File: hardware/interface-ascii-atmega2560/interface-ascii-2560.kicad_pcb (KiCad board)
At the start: 2 copper layers, 88.9 x 132.1 mm, 46 parts, among them J1 Apple 2, J2 Apple 1, J3 UART, J4 Conn_01x05, J5 SOL-20, J6 ISP header, J7 Keyboard, SW1 Options, U1 ATmega2560-16AU, Y1 16.000 MHz

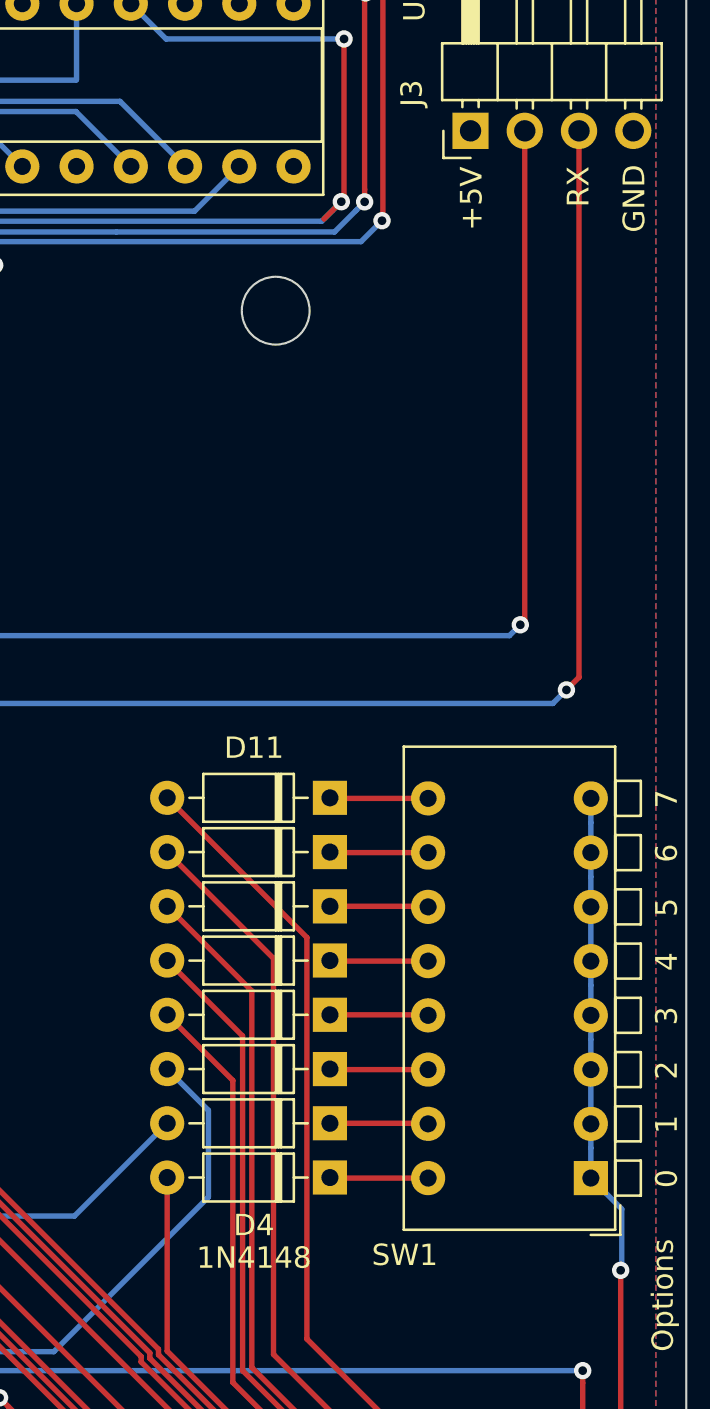
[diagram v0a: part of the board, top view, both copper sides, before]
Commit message: Silk screen cleanups
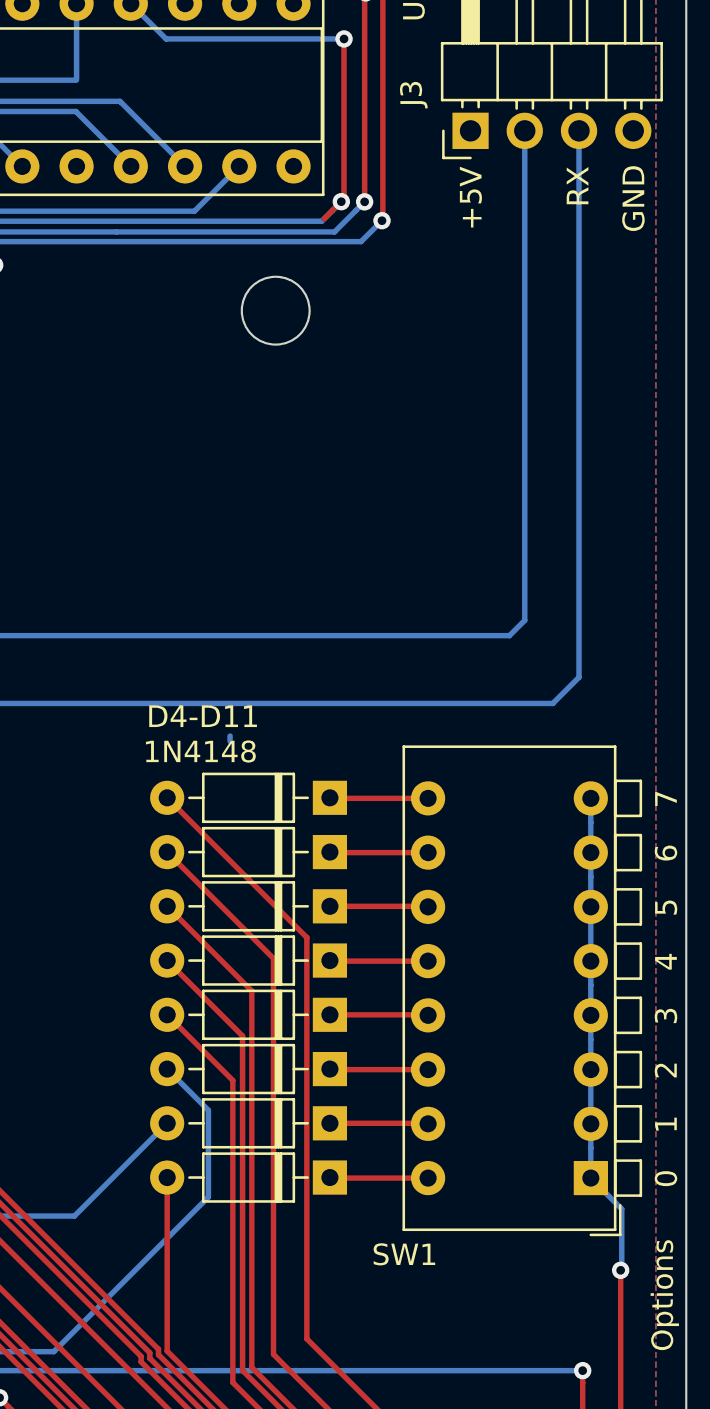
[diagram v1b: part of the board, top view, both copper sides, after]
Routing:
- net /Tx: vias 2 -> 1
- net /Rx: vias 2 -> 1
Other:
- board text added: "D4-D11"

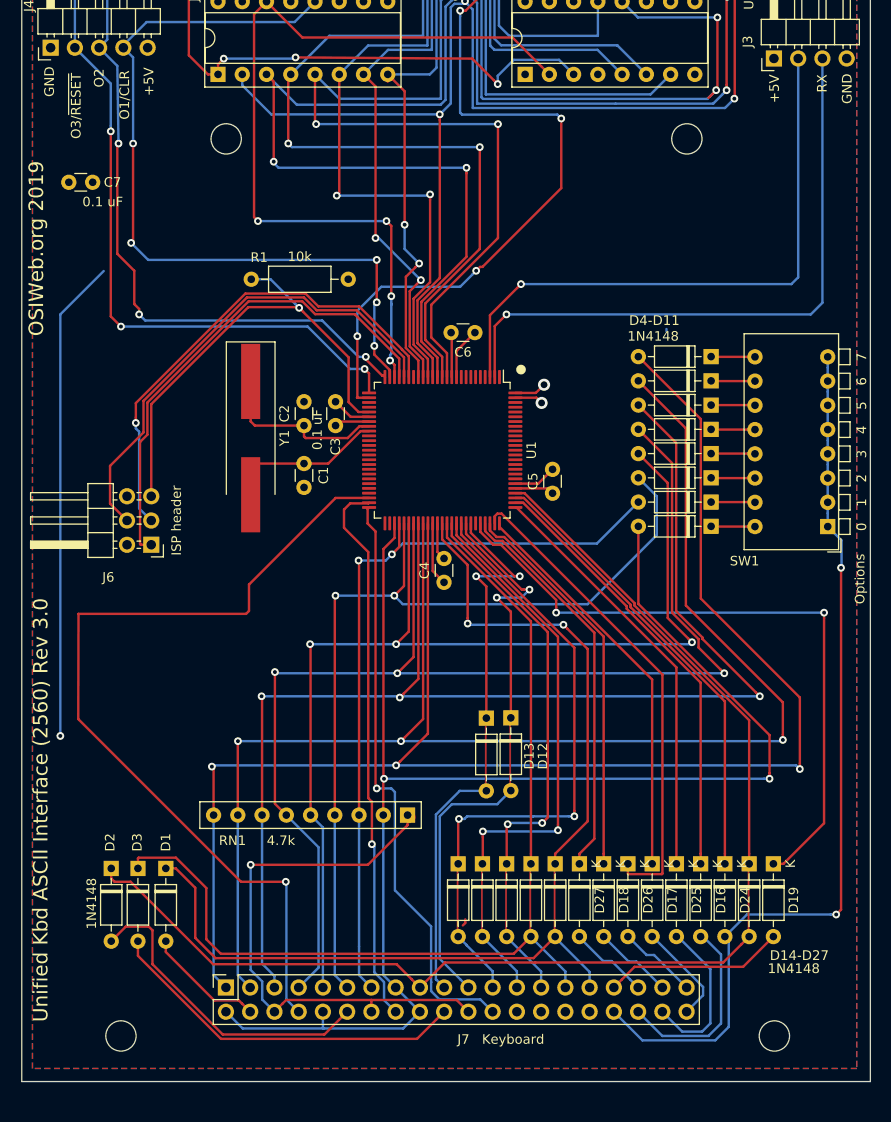
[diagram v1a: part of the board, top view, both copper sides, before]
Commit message: Add 16-pin socket for custom interface/prototyping
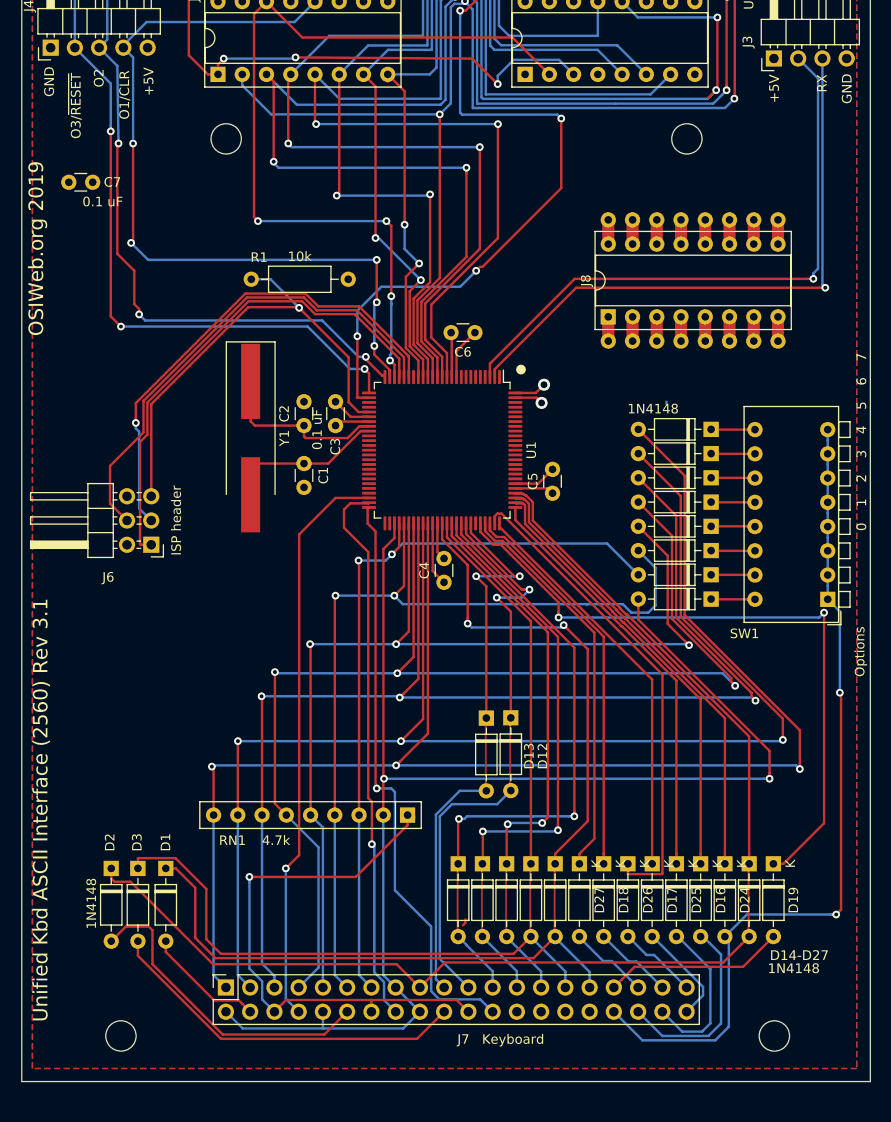
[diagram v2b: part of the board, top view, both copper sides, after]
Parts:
- added J8: Custom Connector / Proto, unikbd:DIP-16_W7.62mm_Proto, F.Cu at (225.3, 102.8)
- moved D10 7.62 mm to (236.0, 117.1)
- moved D11 7.62 mm to (236.0, 114.6)
- moved D4 7.62 mm to (236.0, 132.3)
- moved D5 7.62 mm to (236.0, 129.8)
- moved D6 7.62 mm to (236.0, 127.3)
- moved D8 7.62 mm to (236.0, 122.2)
- moved D7 7.62 mm to (236.0, 124.7)
- moved D9 7.62 mm to (236.0, 119.6)
- moved SW1 7.62 mm to (248.3, 132.4)
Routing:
- net Net-(R2-Pad1): track 50.6 -> 0.00 mm, vias 1 -> 0
- net /LED1: track 91.0 -> 60.0 mm
- net /Col0: track 149.5 -> 141.4 mm
- net /Col3: track 111.9 -> 104.1 mm
- net /Col5: track 138.3 -> 130.5 mm
- net /Col7: track 162.5 -> 154.9 mm
- net /Col6: track 151.2 -> 143.5 mm
- net /Row8: track 95.2 -> 87.6 mm
- net /Col4: track 128.7 -> 124.5 mm
- net /Rx: track 66.3 -> 63.1 mm
- net /Col2: track 93.5 -> 90.9 mm
- net Net-(D19-Pad1): track 70.3 -> 70.9 mm
- net VCC: track 82.3 -> 81.7 mm
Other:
- board text added: "Unified Kbd ASCII Interface (2560) Rev 3.1"
- board text removed: "D4-D11"
- board text removed: "Unified Kbd ASCII Interface (2560) Rev 3.0"

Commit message: Clean up connector labels on ATmel-2560 ASCII interface PCB
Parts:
- added ?: , , F.Cu at (230.4, 88.2)
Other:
- board text added: "Custom Connector"
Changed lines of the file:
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@@
   (general
     (thickness 1.6)
-    (drawings 33)
+    (drawings 34)
     (tracks 1003)
     (zones 0)
-    (modules 47)
+    (modules 48)
     (nets 148)
   )
@@
     (add_net /Col0)
   )
+  (module "" (layer F.Cu)
+    (at 230.355 88.165)
+    (fp_text reference "" (at 225.275 102.77) (layer F.SilkS)
+      (effects (font (size 1.27 1.27) (thickness 0.15)))
+    )
+    (fp_text value "" (at 225.275 102.77) (layer F.SilkS)
+      (effects (font (size 1.27 1.27) (thickness 0.15)))
+    )
+    (fp_text user "Apple 1" (at 228.323 102.77 90) (layer F.SilkS)
+      (effects (font (size 1.27 1.27) (thickness 0.15)))
+    )
+  )
   (module unikbd:DIP-16_W7.62mm_Proto (layer F.Cu)
     (at 225.275 102.77 90)
     (descr "16-lead though-hole mounted DIP package, row spacing 7.62 mm (300 mils), Socket")
     (tags "THT DIP DIL PDIP 2.54mm 7.62mm 300mil Socket")
-    (fp_text reference J8 (at 3.81 -2.33 90) (layer F.SilkS)
+    (fp_text reference J8 (at 8.255 -3.175 180) (layer F.SilkS)
       (effects (font (size 1 1) (thickness 0.15)))
     )
@@
     )
     (fp_text value SOL-20 (at 5.1308 17.5514 180) (layer F.SilkS)
-      (effects (font (size 1 1) (thickness 0.15)))
+      (effects (font (size 1.27 1.27) (thickness 0.1524)))
     )
     (fp_text user %R (at 1.27 11.43) (layer F.Fab)
@@
       (effects (font (size 1 1) (thickness 0.15)))
     )
-    (fp_text value "Apple 2" (at 10.795 9.856168) (layer F.SilkS)
+    (fp_text value "Apple 2" (at 10.16 18.238168) (layer F.SilkS)
       (effects (font (size 1.27 1.27) (thickness 0.15)))
     )
@@
     )
     (fp_text value "Apple 1" (at 10.795 8.372834 180) (layer F.SilkS)
-      (effects (font (size 1.27 1.27) (thickness 0.15)))
+      (effects (font (size 1.27 1.27) (thickness 0.1524)))
     )
     (fp_text user %R (at 9.50214 -0.78486 180) (layer F.SilkS) hide
@@
     )
   )
+  (gr_text "Custom Connector" (at 234.165 90.07) (layer F.SilkS)
+    (effects (font (size 1.27 1.27) (thickness 0.1524)))
+  )
   (gr_circle (center 216.131 108.2945) (end 216.385 108.2945) (layer F.SilkS) (width 0.508))
   (gr_text O2 (at 171.935 77.751 90) (layer F.SilkS)
@@
   (segment (start 209.753328 71.268111) (end 209.753328 70.693375) (width 0.254) (layer B.Cu) (net 8))
   (segment (start 209.958603 81.586401) (end 209.753328 81.381126) (width 0.254) (layer B.Cu) (net 8))
-  (segment (start 210.328064 70.693375) (end 209.753328 70.693375) (width 0.254) (layer F.Cu) (net 8))
-  (segment (start 231.836801 65.855199) (end 229.974 67.718) (width 0.254) (layer F.Cu) (net 8))
-  (segment (start 231.836801 58.531801) (end 231.836801 65.855199) (width 0.254) (layer F.Cu) (net 8))
-  (segment (start 213.303439 67.718) (end 210.328064 70.693375) (width 0.254) (layer F.Cu) (net 8))
-  (segment (start 230.6598 57.3548) (end 231.836801 58.531801) (width 0.254) (layer F.Cu) (net 8))
-  (segment (start 229.974 67.718) (end 213.303439 67.718) (width 0.254) (layer F.Cu) (net 8))
   (segment (start 200.2135 111.24) (end 198.947 111.24) (width 0.254) (layer F.Cu) (net 8))
   (segment (start 198.947 111.24) (end 198.986 111.201) (width 0.254) (layer F.Cu) (net 8))
@@
   (segment (start 212.091385 97.537601) (end 211.838399 97.537601) (width 0.254) (layer F.Cu) (net 8))
   (segment (start 211.838399 97.537601) (end 211.432 97.944) (width 0.254) (layer F.Cu) (net 8))
+  (segment (start 210.328064 70.693375) (end 209.753328 70.693375) (width 0.254) (layer F.Cu) (net 8))
+  (segment (start 213.303439 67.718) (end 210.328064 70.693375) (width 0.254) (layer F.Cu) (net 8))
+  (segment (start 230.6598 57.3548) (end 231.836801 58.531801) (width 0.254) (layer F.Cu) (net 8))
+  (segment (start 229.9105 67.718) (end 213.303439 67.718) (width 0.254) (layer F.Cu) (net 8))
+  (segment (start 231.836801 65.791699) (end 229.9105 67.718) (width 0.254) (layer F.Cu) (net 8))
+  (segment (start 231.836801 58.531801) (end 231.836801 65.791699) (width 0.254) (layer F.Cu) (net 8))
   (via (at 206.4028 66.3718) (size 0.8128) (drill 0.4064) (layers F.Cu B.Cu) (net 9))
   (segment (start 192.010166 77.37) (end 196.048766 73.3314) (width 0.254) (layer B.Cu) (net 9))
